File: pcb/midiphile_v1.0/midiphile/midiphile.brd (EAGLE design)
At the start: 160 x 100 mm, 9 parts

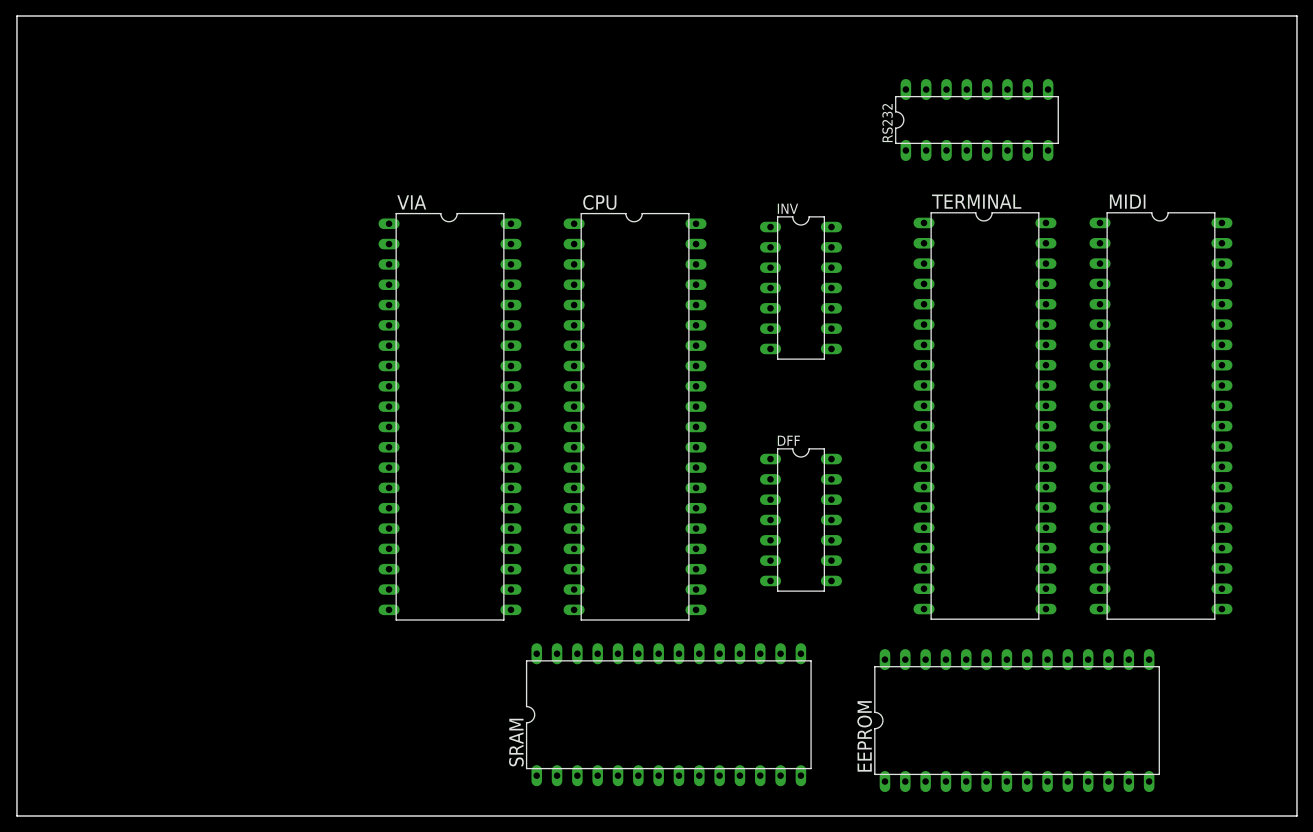
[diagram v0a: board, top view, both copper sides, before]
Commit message: Add PLCC packages for 65c02 and 16550; roughly lay out ICs on board
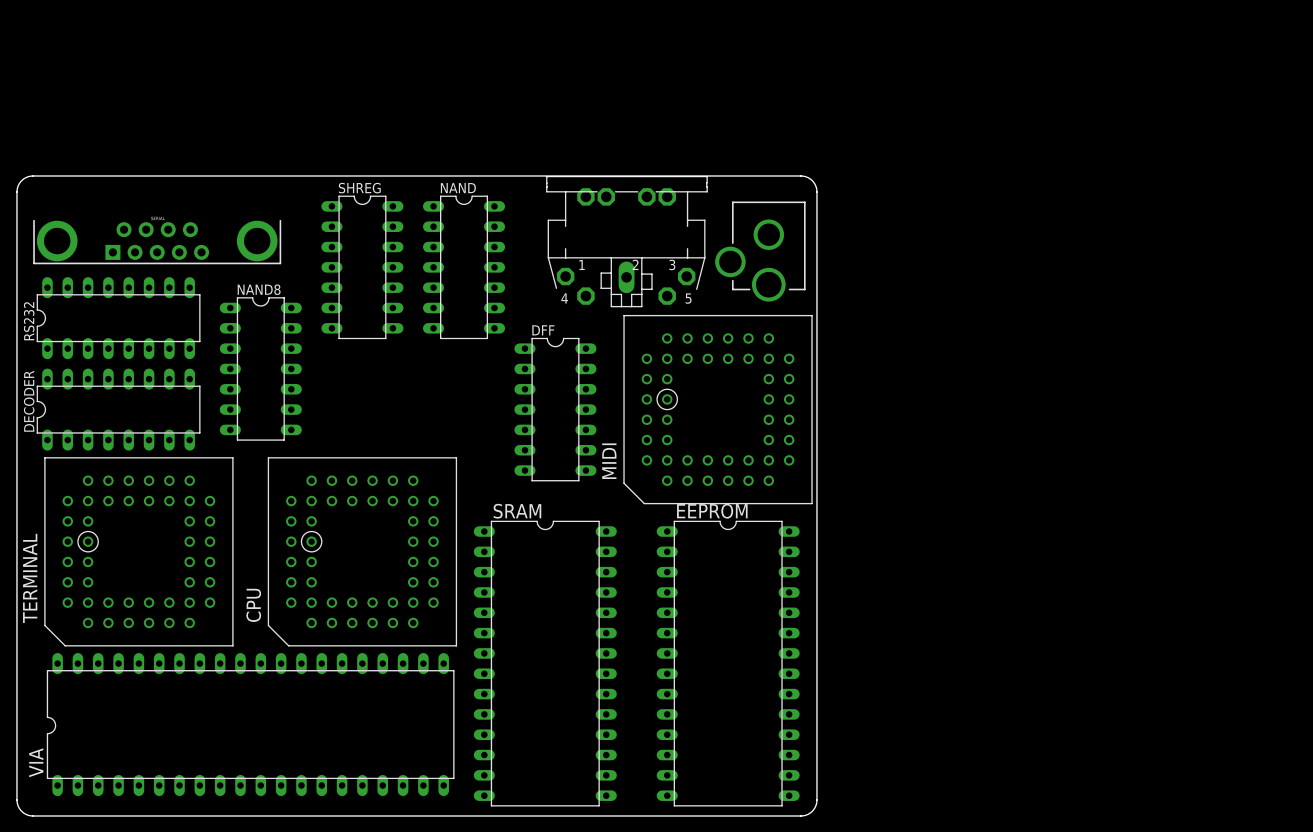
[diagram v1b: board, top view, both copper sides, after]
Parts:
- removed INV: 74LS06N, 74xx-us:DIL14
- added DECODER: 74LS138N, 74xx-us:DIL16
- added DIN: MIDIJACK, adafruit:CP-2350
- added NAND: 74LS00N, 74xx-us:DIL14
- added NAND8: 74LS30N, 74xx-us:DIL14
- added PWR: (no value), adafruit:DCJACK_2MM_PTH
- added SERIAL: (no value), SparkFun-Connectors:DB9_MALE
- added SHREG: 74HC164N, 74xx-us:DIL14
- CPU: value W65C02S6TP -> W65C02S6TPLG; device 6502:DIL40 -> 6502:PLCC44SOCKET
- MIDI, TERMINAL: value PC16550DN -> PC16550DV; device 16550:DIL40 -> 16550:PLCC44SOCKET
- moved RS232 110.1 mm to (12.7, 62.2)
- moved TERMINAL 107.1 mm to (15.2, 33.0), turned to 90 degrees
- moved MIDI 55.4 mm to (87.6, 50.8), turned to 90 degrees
- moved VIA 45.8 mm to (29.2, 11.4), turned to 0 degrees
- moved CPU 38.0 mm to (43.2, 33.0), turned to 90 degrees
- moved EEPROM 36.8 mm to (88.9, 19.1), turned to 270 degrees
- moved DFF 33.6 mm to (67.3, 50.8)
- moved SRAM 16.7 mm to (66.0, 19.1), turned to 270 degrees
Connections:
- new net !IRQB!: CPU.5
- new net !MIDISEL!: DECODER.13, MIDI.16
- new net !MRD!: EEPROM.22, MIDI.24, NAND.3, NAND.4, SRAM.22, TERMINAL.24
- new net !MWR!: MIDI.20, NAND.6, SRAM.27, TERMINAL.20
- new net !NMIB!: CPU.7, VIA.21
- new net !RAMSEL!: NAND.11, SRAM.20
- new net !RESB!: CPU.44, DFF.4, VIA.34
- new net !ROMSEL!: EEPROM.20, NAND.12, NAND.8
- new net !TERMSEL!: DECODER.14, TERMINAL.16
- new net !VIASEL!: DECODER.15, VIA.23
- new net +5V: CPU.37, CPU.9, DECODER.16, MIDI.44, NAND.14, RS232.2, SHREG.14, TERMINAL.44
- new net A0: CPU.10, EEPROM.10, MIDI.31, SRAM.21, TERMINAL.31, VIA.38
- new net A1: CPU.11, EEPROM.9, MIDI.30, SRAM.23, TERMINAL.30, VIA.37
- new net A10: CPU.21, EEPROM.21, NAND8.5, SRAM.6
- new net A11: CPU.22, EEPROM.23, NAND8.4, SRAM.7
- new net A12: CPU.25, EEPROM.2, NAND8.3, SRAM.8
- new net A13: CPU.26, EEPROM.26, NAND8.2, SRAM.9
- new net A14: CPU.27, EEPROM.1, NAND8.1, SRAM.10
- new net A15: CPU.28, DECODER.4, NAND.10, NAND.9
- new net A2: CPU.13, EEPROM.8, MIDI.29, SRAM.24, TERMINAL.29, VIA.36
- new net A3: CPU.14, EEPROM.7, SRAM.25, VIA.35
- new net A4: CPU.15, DECODER.1, EEPROM.6, SRAM.26
- new net A5: CPU.16, DECODER.2, EEPROM.5, SRAM.1
- new net A6: CPU.17, DECODER.3, EEPROM.4, SRAM.2
- new net A7: CPU.18, EEPROM.3, NAND8.12, SRAM.3
- new net A8: CPU.19, EEPROM.25, NAND8.11, SRAM.4
- new net A9: CPU.20, EEPROM.24, NAND8.6, SRAM.5
- new net D0: CPU.36, EEPROM.11, MIDI.2, SRAM.11, TERMINAL.2, VIA.33
- new net D1: CPU.35, EEPROM.12, MIDI.3, SRAM.12, TERMINAL.3, VIA.32
- new net D2: CPU.34, EEPROM.13, MIDI.4, SRAM.13, TERMINAL.4, VIA.31
- new net D3: CPU.33, EEPROM.15, MIDI.5, SRAM.15, TERMINAL.5, VIA.30
- new net D4: CPU.32, EEPROM.16, MIDI.6, SRAM.16, TERMINAL.6, VIA.29
- new net D5: CPU.31, EEPROM.17, MIDI.7, SRAM.17, TERMINAL.7, VIA.28
- new net D6: CPU.30, EEPROM.18, MIDI.8, SRAM.18, TERMINAL.8, VIA.27
- new net D7: CPU.29, EEPROM.19, MIDI.9, SRAM.19, TERMINAL.9, VIA.26
- new net GNDBREAK: PWR.GNDBREAK
- new net MISO: SHREG.2
- new net MOSI: VIA.19
- new net N$10: SHREG.6, VIA.13
- new net N$11: SHREG.10, VIA.14
- new net N$12: SHREG.11, VIA.15
- new net N$13: SHREG.12, VIA.16
- new net N$14: SHREG.13, VIA.17
- new net N$15: DFF.2, VIA.18
- new net N$16: RS232.11, TERMINAL.13
- new net N$17: DFF.5, SHREG.8
- new net N$18: RS232.12, TERMINAL.11
- new net N$19: RS232.10, TERMINAL.36
- new net N$2: DECODER.5, NAND.13, NAND8.8
- new net N$20: RS232.9, TERMINAL.40
- new net N$21: RS232.14, SERIAL.3
- new net N$22: RS232.13, SERIAL.2
- new net N$23: RS232.7, SERIAL.7
- new net N$24: RS232.8, SERIAL.8
- new net N$3: MIDI.33
- new net N$4: TERMINAL.33
- new net N$5: MIDI.10, MIDI.17
- new net N$6: TERMINAL.10, TERMINAL.17
- new net N$7: SHREG.3, VIA.10
- new net N$8: SHREG.4, VIA.11
- new net N$9: SHREG.5, VIA.12
- new net PHI2: CPU.43, DFF.3, MIDI.18, NAND.5, VIA.25
- new net PWR: PWR.PWR
- new net R!WB!: CPU.38, NAND.1, NAND.2, VIA.22
- new net SCK: DFF.6
- net GND: now also CPU.1, CPU.23, CPU.24, DECODER.8, MIDI.21, MIDI.22, MIDI.25, MIDI.28, NAND.7, NAND8.7, PWR.GND, RS232.6, SERIAL.5, SHREG.7, TERMINAL.21, TERMINAL.22, TERMINAL.25, TERMINAL.28; no longer INV.7
- net VCC: now also DECODER.6, DFF.1, EEPROM.27, MIDI.14, MIDI.15, NAND8.14, SHREG.1, SHREG.9, TERMINAL.14, TERMINAL.15, VIA.24; no longer INV.14
- net VDD: no longer CPU.8, MIDI.40, TERMINAL.40
- net VSS: no longer CPU.21, MIDI.20, TERMINAL.20
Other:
- board size 160 x 100 mm -> 100 x 80 mm

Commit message: Add oscillators, reset and nmi, and thinner sram
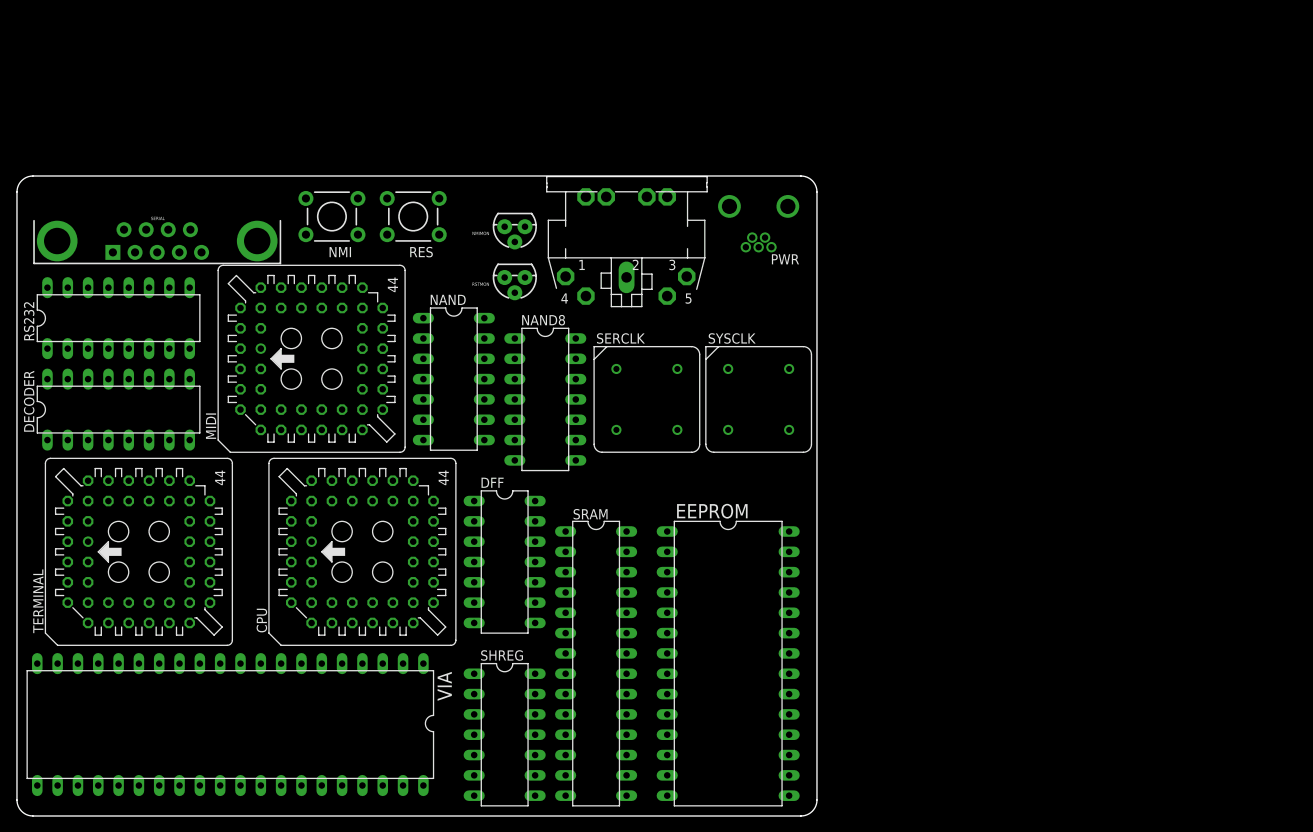
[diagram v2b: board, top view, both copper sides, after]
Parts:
- added NMI, RES: SWITCH-MOMENTARY-2PTH, SparkFun-Electromechanical:TACTILE-PTH
- added NMIMON, RSTMON: DS1813, ds1813:TO-92
- added SERCLK: 1.8432M, metal_can_oscillator:HALF_CAN_SOCKET
- added SYSCLK: 1M, metal_can_oscillator:HALF_CAN_SOCKET
- CPU: device 6502:PLCC44SOCKET -> 6502:S44
- MIDI, TERMINAL: device 16550:PLCC44SOCKET -> 16550:S44
- PWR: value (none) -> USB-MB-H; device adafruit:DCJACK_2MM_PTH -> SparkFun-Connectors:USB-MB-H
- SRAM: value 62256 -> 71256SA20TPG; device 62xxx_sram:DIL28 -> 71xxx_sram:DIL28-3
- moved SHREG 61.1 mm to (61.0, 10.2)
- moved MIDI 51.2 mm to (36.8, 57.1)
- moved NAND8 35.8 mm to (66.0, 52.1)
- moved DFF 20.1 mm to (61.0, 31.8)
- moved NAND 14.0 mm to (54.6, 54.6)
- moved SRAM 6.35 mm to (72.4, 19.1)
- moved PWR 4.02 mm to (92.7, 76.2), turned to 270 degrees
- moved VIA 2.54 mm to (26.7, 11.4), turned to 180 degrees
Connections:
- removed net !NMIB!: CPU.7, VIA.21
- removed net GNDBREAK: PWR.GNDBREAK
- removed net PWR: PWR.PWR
- new net N$1: CPU.1, NMI.3, NMIMON.1
- new net N$25: SERCLK.5, TERMINAL.18
- net !IRQB!: now also CPU.43, VIA.21; no longer CPU.5
- net !RESB!: now also CPU.38, RES.1, RSTMON.1; no longer CPU.44
- net +5V: now also CPU.3, CPU.31, EEPROM.28, SRAM.28; no longer CPU.37, CPU.9
- net A0: now also CPU.4, SRAM.10; no longer CPU.10, SRAM.21
- net A1: now also CPU.5, SRAM.9; no longer CPU.11, SRAM.23
- net A10: now also CPU.15, SRAM.21; no longer CPU.21, SRAM.6
- net A11: now also CPU.16, SRAM.23; no longer CPU.22, SRAM.7
- net A12: now also CPU.19, SRAM.2; no longer CPU.25, SRAM.8
- net A13: now also CPU.20, SRAM.26; no longer CPU.26, SRAM.9
- net A14: now also CPU.21, SRAM.1; no longer CPU.27, SRAM.10
- net A15: now also CPU.22; no longer CPU.28
- net A2: now also CPU.7, SRAM.8; no longer CPU.13, SRAM.24
- net A3: now also CPU.8, SRAM.7; no longer CPU.14, SRAM.25
- net A4: now also CPU.9, SRAM.6; no longer CPU.15, SRAM.26
- net A5: now also CPU.10, SRAM.5; no longer CPU.16, SRAM.1
- net A6: now also CPU.11, SRAM.4; no longer CPU.17, SRAM.2
- net A7: now also CPU.12; no longer CPU.18
- net A8: now also CPU.13, SRAM.25; no longer CPU.19, SRAM.4
- net A9: now also CPU.14, SRAM.24; no longer CPU.20, SRAM.5
- net D0: now also CPU.30; no longer CPU.36
- net D1: now also CPU.29; no longer CPU.35
- net D2: now also CPU.28; no longer CPU.34
- net D3: now also CPU.27; no longer CPU.33
- net D4: now also CPU.26; no longer CPU.32
- net D5: now also CPU.25; no longer CPU.31
- net D6: now also CPU.24; no longer CPU.30
- net D7: now also CPU.23; no longer CPU.29
- net GND: now also CPU.17, CPU.18, CPU.39, EEPROM.14, NMI.1, NMIMON.3, RES.3, RSTMON.3, SERCLK.4, SRAM.14, SYSCLK.4; no longer CPU.1, CPU.23, CPU.24, PWR.GND
- net PHI2: now also CPU.35, SYSCLK.5; no longer CPU.43
- net R!WB!: now also CPU.32; no longer CPU.38
- net VCC: now also NMIMON.2, RSTMON.2, SERCLK.8, SYSCLK.8
- net VDD: no longer SRAM.28
- net VSS: no longer SRAM.14

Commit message: Add 16C2552, expansion headers, rectangular LEDs
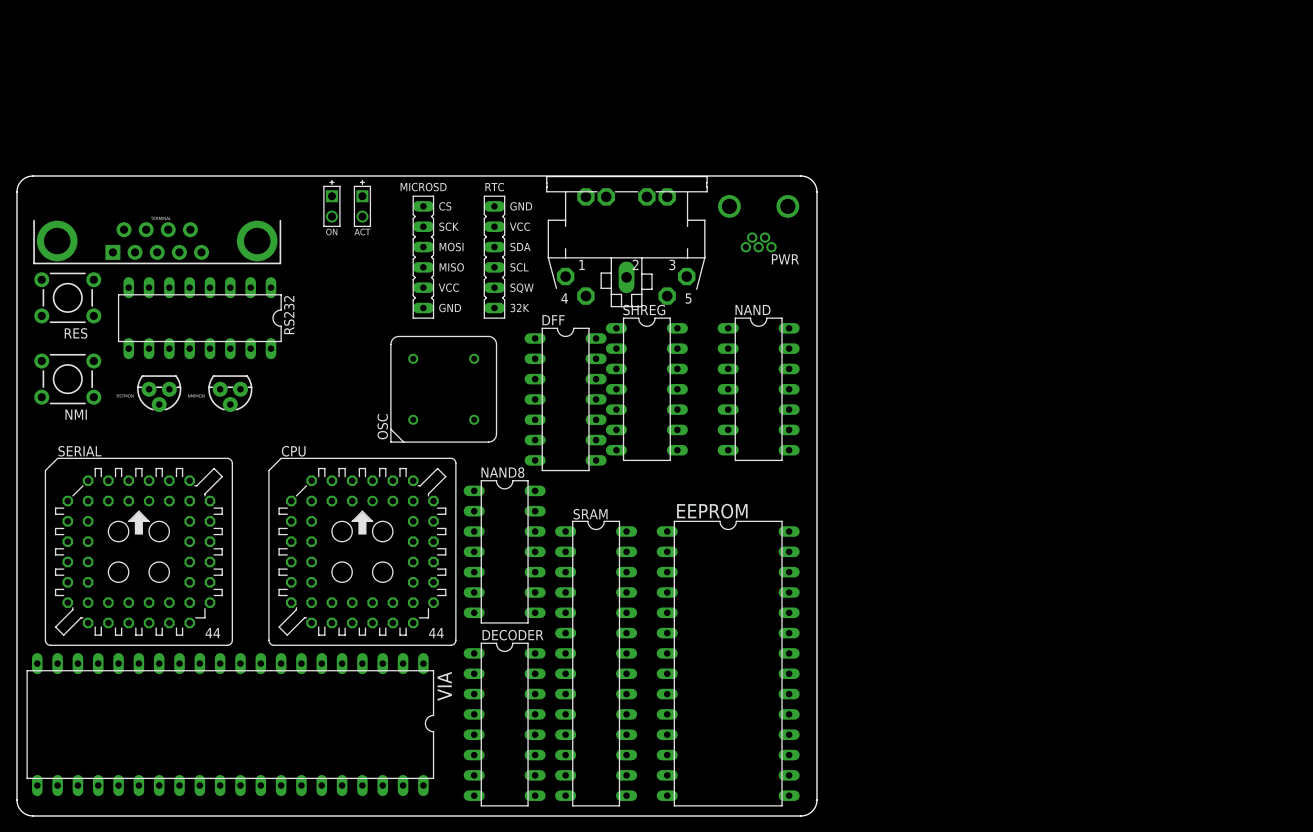
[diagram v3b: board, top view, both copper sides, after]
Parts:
- removed MIDI: PC16550DV, 16550:S44
- removed SERCLK: 1.8432M, metal_can_oscillator:HALF_CAN_SOCKET
- removed SYSCLK: 1M, metal_can_oscillator:HALF_CAN_SOCKET
- added ACT: AMBER, led:LED_RECT_2X5MM
- added MICROSD: FE06-SPI-USD, expansion_headers:FE06-SPI-USD
- added ON: RED, led:LED_RECT_2X5MM
- added OSC: 24M, metal_can_oscillator:HALF_CAN_SOCKET
- added RTC: FE06-I2C-RTC, expansion_headers:FE06-I2C-RTC
- SERIAL: value (none) -> ST16C2552CJ44-F; device SparkFun-Connectors:DB9_MALE -> 16550:S44
- TERMINAL: value PC16550DV -> (none); device 16550:S44 -> SparkFun-Connectors:DB9_MALE
- moved DECODER 62.3 mm to (61.0, 11.4), turned to 270 degrees
- moved SHREG 46.7 mm to (78.7, 53.3)
- moved RSTMON 46.6 mm to (17.8, 53.3)
- moved RES 44.4 mm to (6.35, 64.8)
- moved NMIMON 41.0 mm to (26.7, 53.3)
- moved SERIAL 38.9 mm to (15.2, 33.0)
- moved TERMINAL 38.9 mm to (17.5, 71.9), turned to 0 degrees
- moved NMI 38.8 mm to (6.35, 54.6)
- moved NAND 38.1 mm to (92.7, 53.3)
- moved DFF 21.7 mm to (68.6, 52.1)
- moved NAND8 19.7 mm to (61.0, 33.0)
- moved RS232 10.2 mm to (22.9, 62.2), turned to 180 degrees
- turned CPU to 0 degrees
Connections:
- removed net !MIDISEL!: DECODER.13, MIDI.16
- removed net !TERMSEL!: DECODER.14, TERMINAL.16
- removed net N$16: RS232.11, TERMINAL.13
- removed net N$18: RS232.12, TERMINAL.11
- removed net N$19: RS232.10, TERMINAL.36
- removed net N$20: RS232.9, TERMINAL.40
- removed net N$25: SERCLK.5, TERMINAL.18
- removed net N$6: TERMINAL.10, TERMINAL.17
- new net !CTS!: RS232.9
- new net !RTS!: RS232.10
- new net !SERSEL!: DECODER.14, SERIAL.18
- new net CS0: VIA.6
- new net CS1: VIA.7
- new net RX: RS232.12
- new net SCL: VIA.8
- new net SDA: VIA.9
- new net TX: RS232.11
- net !MRD!: now also SERIAL.24; no longer MIDI.24, TERMINAL.24
- net !MWR!: now also SERIAL.20; no longer MIDI.20, TERMINAL.20
- net +5V: now also SERIAL.33, SERIAL.44; no longer MIDI.44, TERMINAL.44
- net A0: now also SERIAL.10; no longer MIDI.31, TERMINAL.31
- net A1: now also SERIAL.14; no longer MIDI.30, TERMINAL.30
- net A2: now also SERIAL.15; no longer MIDI.29, TERMINAL.29
- net A3: now also SERIAL.16
- net D0: now also SERIAL.2; no longer MIDI.2, TERMINAL.2
- net D1: now also SERIAL.3; no longer MIDI.3, TERMINAL.3
- net D2: now also SERIAL.4; no longer MIDI.4, TERMINAL.4
- net D3: now also SERIAL.5; no longer MIDI.5, TERMINAL.5
- net D4: now also SERIAL.6; no longer MIDI.6, TERMINAL.6
- net D5: now also SERIAL.7; no longer MIDI.7, TERMINAL.7
- net D6: now also SERIAL.8; no longer MIDI.8, TERMINAL.8
- net D7: now also SERIAL.9; no longer MIDI.9, TERMINAL.9
- net GND: now also OSC.4, SERIAL.12, SERIAL.22, TERMINAL.5; no longer MIDI.21, MIDI.22, MIDI.25, MIDI.28, SERCLK.4, SERIAL.5, SYSCLK.4, TERMINAL.21, TERMINAL.22, TERMINAL.25, TERMINAL.28
- net N$21: now also TERMINAL.3; no longer SERIAL.3
- net N$22: now also TERMINAL.2; no longer SERIAL.2
- net N$23: now also TERMINAL.7; no longer SERIAL.7
- net N$24: now also TERMINAL.8; no longer SERIAL.8
- net N$3: now also SERIAL.17, VIA.39; no longer MIDI.33
- net N$4: now also SERIAL.34, VIA.40; no longer TERMINAL.33
- net N$5: now also SERIAL.21, VIA.2; no longer MIDI.10, MIDI.17
- net PHI2: no longer MIDI.18, SYSCLK.5
- net VCC: now also OSC.8; no longer MIDI.14, MIDI.15, SERCLK.8, SYSCLK.8, TERMINAL.14, TERMINAL.15
